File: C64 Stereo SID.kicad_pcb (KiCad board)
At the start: 2 copper layers, 48.9 x 41.9 mm, 16 parts, among them J1 EXT_IN_SEL1, J2 EXT_IN_SEL2, J3 AUD_OUT2, J4 ~CS, Q1 2N2222, U1 MOS_6581, U2 MOS_6581

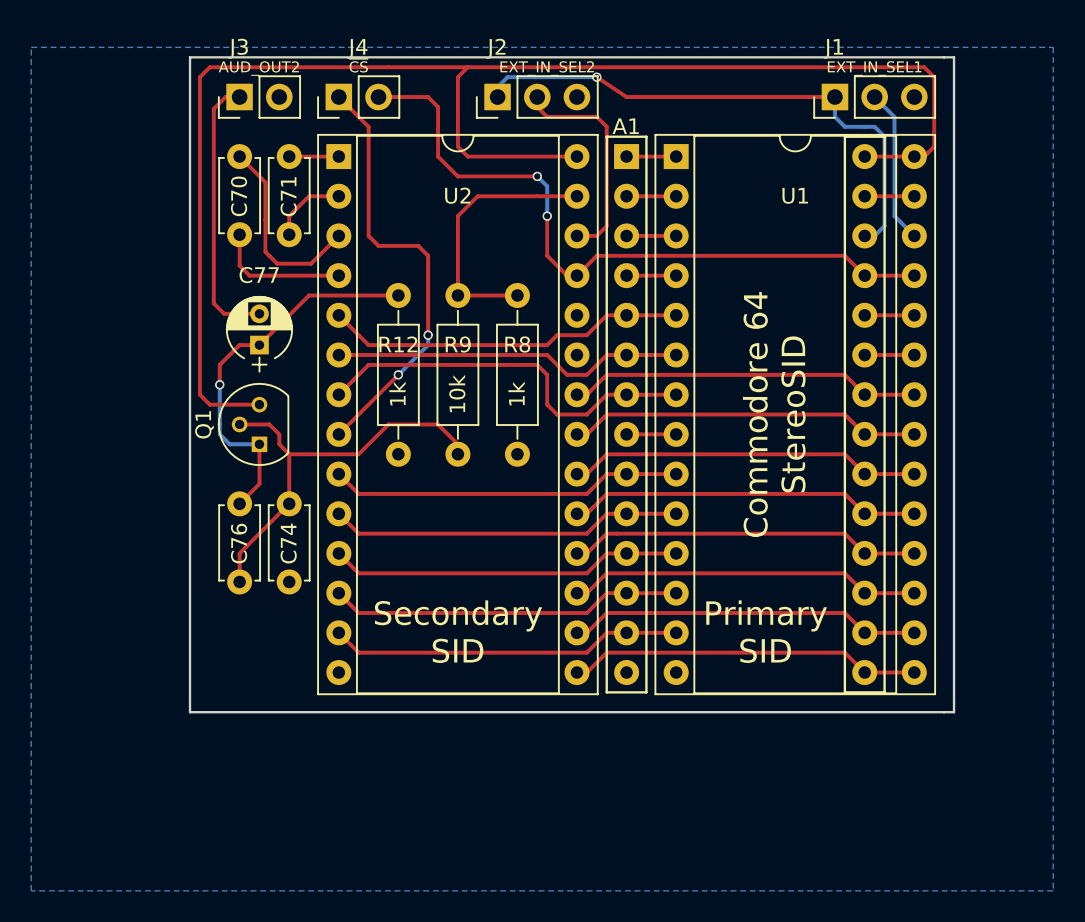
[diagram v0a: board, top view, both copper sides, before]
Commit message: Added header for swapping SIDs around
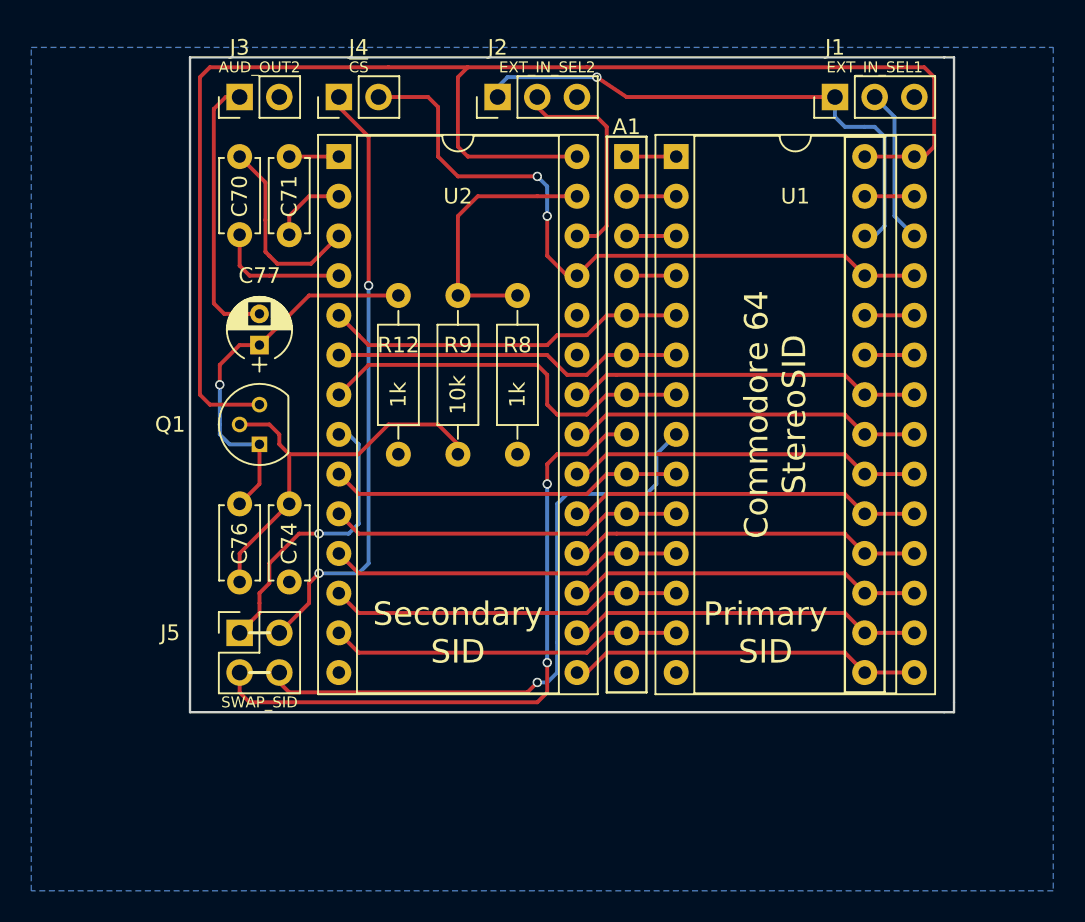
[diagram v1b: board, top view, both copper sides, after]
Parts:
- added J5: SWAP_SID, Pin_Headers:Pin_Header_Straight_2x02_Pitch2.54mm, F.Cu at (102.2, 134.6)
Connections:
- A1 pad 8: /~CS -> ~CS1_IN
- J4 pad 1: ~CS2 -> ~CS2_IN
- U1 pad 8: /~CS -> ~CS1_IC
- U2 pad 8: ~CS2 -> ~CS2_IC
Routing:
- net ~CS1_IN: track 0.00 -> 42.0 mm, vias 0 -> 2
- net ~CS1_IC: track 0.00 -> 40.6 mm, vias 0 -> 1
- net ~CS2_IN: track 0.00 -> 38.9 mm, vias 0 -> 2
- net ~CS2: track 29.7 -> 0.00 mm, vias 2 -> 0
- net ~CS2_IC: track 0.00 -> 19.9 mm, vias 0 -> 1
- net /~CS: track 3.18 -> 0.00 mm

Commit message: Changed to select SIDs as pseudo stereo
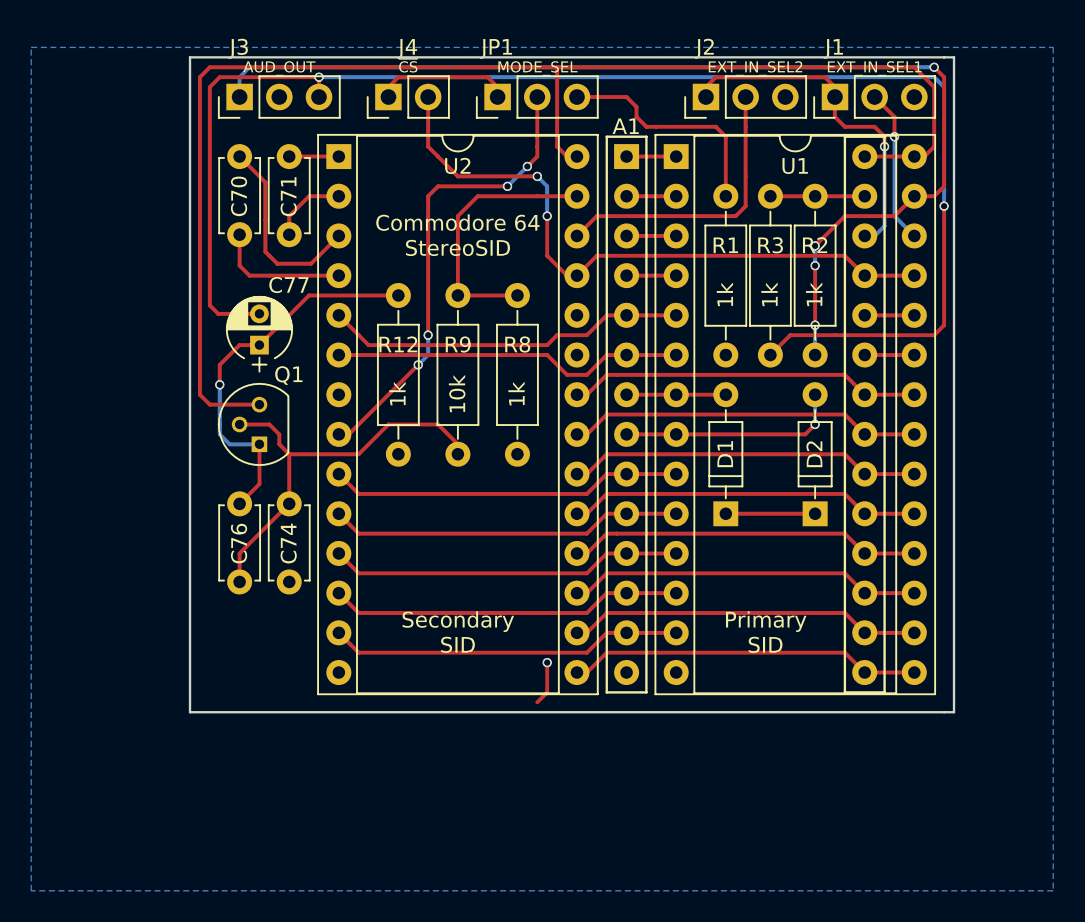
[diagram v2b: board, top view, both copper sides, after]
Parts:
- removed J5: SWAP_SID, Pin_Headers:Pin_Header_Straight_2x02_Pitch2.54mm
- added D1: 1N4148, Diodes_THT:D_DO-35_SOD27_P7.62mm_Horizontal, F.Cu at (133.3, 127.0)
- added D2: 1N4148, Diodes_THT:D_DO-35_SOD27_P7.62mm_Horizontal, F.Cu at (139.1, 127.0)
- added JP1: MODE_SEL, Pin_Headers:Pin_Header_Straight_1x03_Pitch2.54mm, F.Cu at (118.7, 100.3)
- added R1: 1k, Resistors_THT:R_Axial_DIN0207_L6.3mm_D2.5mm_P10.16mm_Horizontal, F.Cu at (133.3, 106.7)
- added R2: 1k, Resistors_THT:R_Axial_DIN0207_L6.3mm_D2.5mm_P10.16mm_Horizontal, F.Cu at (139.1, 106.7)
- added R3: 1k, Resistors_THT:R_Axial_DIN0207_L6.3mm_D2.5mm_P10.16mm_Horizontal, F.Cu at (136.2, 106.7)
- C70, C71: value 470pF -> 470pF*
- J3: value AUD_OUT2 -> AUD_OUT; footprint Pin_Headers:Pin_Header_Straight_1x02_Pitch2.54mm -> Pin_Headers:Pin_Header_Straight_1x03_Pitch2.54mm
- moved J2 13.3 mm to (132.1, 100.3)
- moved J4 3.18 mm to (111.8, 100.3)
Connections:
- A1 pad 27: /AUD_OUT -> AUD_OUT
- A1 pad 7: /R/~W -> R/~W
- C77 pad 2: Net-(C77-Pad2) -> AUD_R
- J3 pad 1: Net-(C77-Pad2) -> AUD_L
- U1 pad 27: /AUD_OUT -> AUD_L
- U1 pad 7: /R/~W -> R/~W
- U1 pad 8: ~CS1_IC -> ~CS1_IN
- U2 pad 7: /R/~W -> GND
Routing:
- net AUD_R: track 0.00 -> 93.3 mm, vias 0 -> 2
- net AUD_L: track 0.00 -> 70.7 mm, vias 0 -> 4
- net ~CS1_IC: track 40.6 -> 0.00 mm, vias 1 -> 0
- net ~CS2_IN: track 38.9 -> 10.1 mm, vias 2 -> 0
- net ~CS1_IN: track 42.0 -> 14.2 mm, vias 2 -> 1
- net /R/~W: track 25.3 -> 0.00 mm
- net Net-(D1-Pad1): track 0.00 -> 20.5 mm
- net Net-(C77-Pad2): track 17.6 -> 0.00 mm
- net /EXT_IN: track 35.1 -> 22.3 mm
- net ~CS2_IC: track 19.9 -> 31.1 mm, vias 1 -> 4
- net VDD: track 94.3 -> 87.3 mm
- net R/~W: track 0.00 -> 6.35 mm
- net AUD_OUT: track 0.00 -> 6.03 mm
- net EXT_IN2: track 14.1 -> 18.6 mm
- net VCC: track 44.5 -> 41.4 mm
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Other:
- board text added: "AUD_OUT 1- 2- 3-"
- board text added: "EXT_IN_SEL1/2 1-2 2-3"
- board text added: "Left"
- board text added: "MODE_SEL 1-2 Messiah 2-3 Dual SID"
- board text added: "Right"
- board text removed: "AUD_OUT2 1- 2-"
- board text removed: "EXT_IN_SEL1/2 NC 1-2 2-3"
- board text removed: "None"
- board text removed: "Right channel"
